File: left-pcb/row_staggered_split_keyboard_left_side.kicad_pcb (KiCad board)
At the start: 2 copper layers, 165 x 132 mm, 177 parts, among them J1 Conn_01x02, SW1 SW_SPST, SW10 SW_SPST, SW11 SW_SPST, SW12 SW_SPST, SW13 SW_SPST, SW14 SW_SPST, SW15 SW_SPST, SW16 SW_SPST, SW17 SW_SPST, SW18 SW_SPST, SW19 SW_SPST, SW2 SW_SPST, SW20 SW_SPST, SW21 SW_SPST, SW22 SW_SPST, SW23 SW_SPST, SW24 SW_SPST, SW25 SW_SPST, SW26 SW_SPST, SW27 SW_SPST, SW28 SW_SPST, SW29 SW_SPST, SW3 SW_SPST, SW30 SW_SPST, SW31 SW_SPST, SW32 SW_SPST, SW33 SW_SPST, SW34 SW_SPST, SW35 SW_SPST, SW36 SW_SPST, SW37 SW_SPST, SW38 SW_SPST, SW39 SW_SPST, SW4 SW_SPST, SW40 SW_SPST, SW41 SW_SPST, SW5 SW_SPST, SW6 SW_SPST, SW7 SW_SPST, SW8 SW_SPST, SW9 SW_SPST, U1 SN74LVC1T45DBV

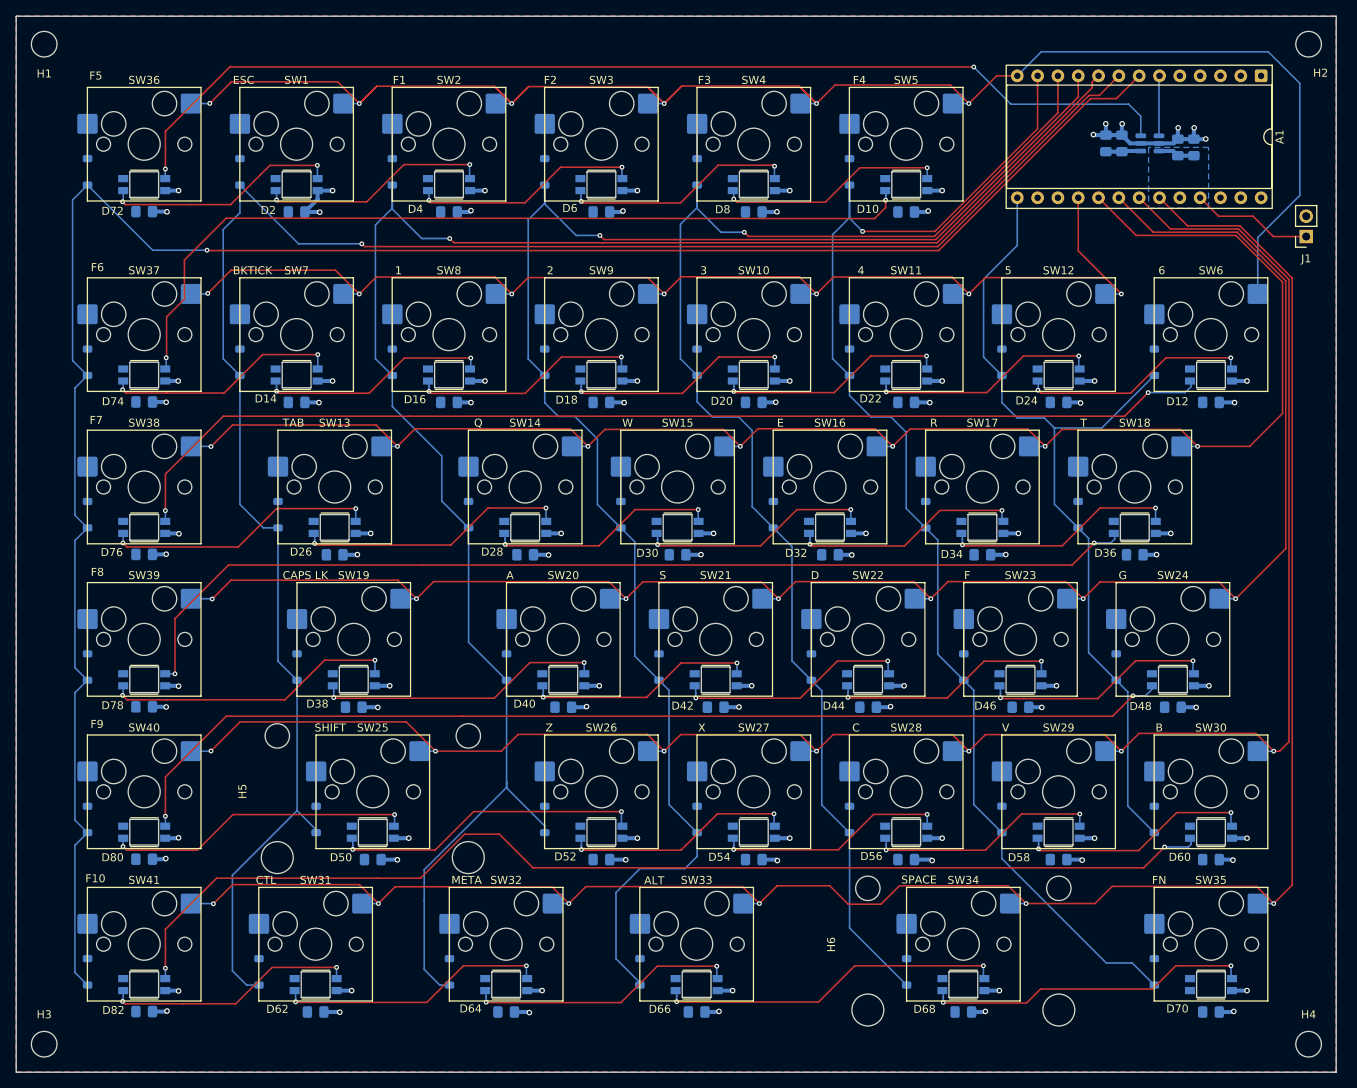
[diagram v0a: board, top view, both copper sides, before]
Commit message: reworking LED data lines to eliminate ground plane disconnections
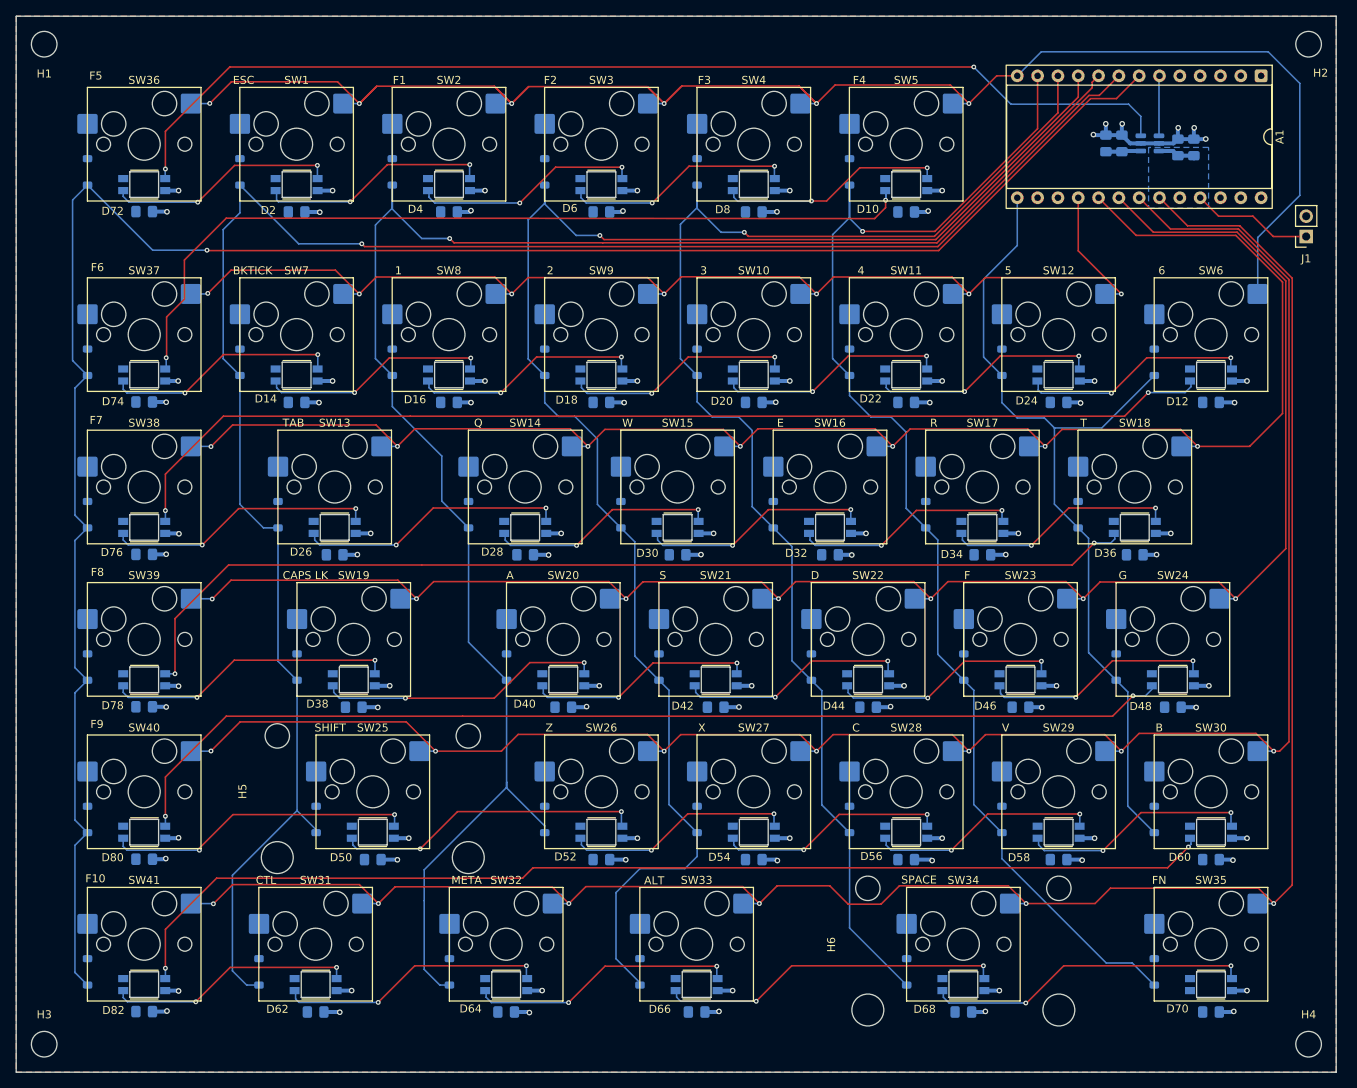
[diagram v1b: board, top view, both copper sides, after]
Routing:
- net /R5C6/DOUT: track 143.0 -> 139.5 mm
- net GND: track 179.3 -> 176.0 mm
- net /R1C0/DOUT: track 29.6 -> 28.9 mm
- net /R6C0/DOUT: track 31.5 -> 31.0 mm
- net /R4C0/DOUT: track 36.8 -> 36.2 mm
- net /R1C3/DOUT: track 29.2 -> 28.7 mm
- net /R4C3/DOUT: track 29.1 -> 28.6 mm

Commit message: duplicate track cleanup and avoiding silkscreen with tracks
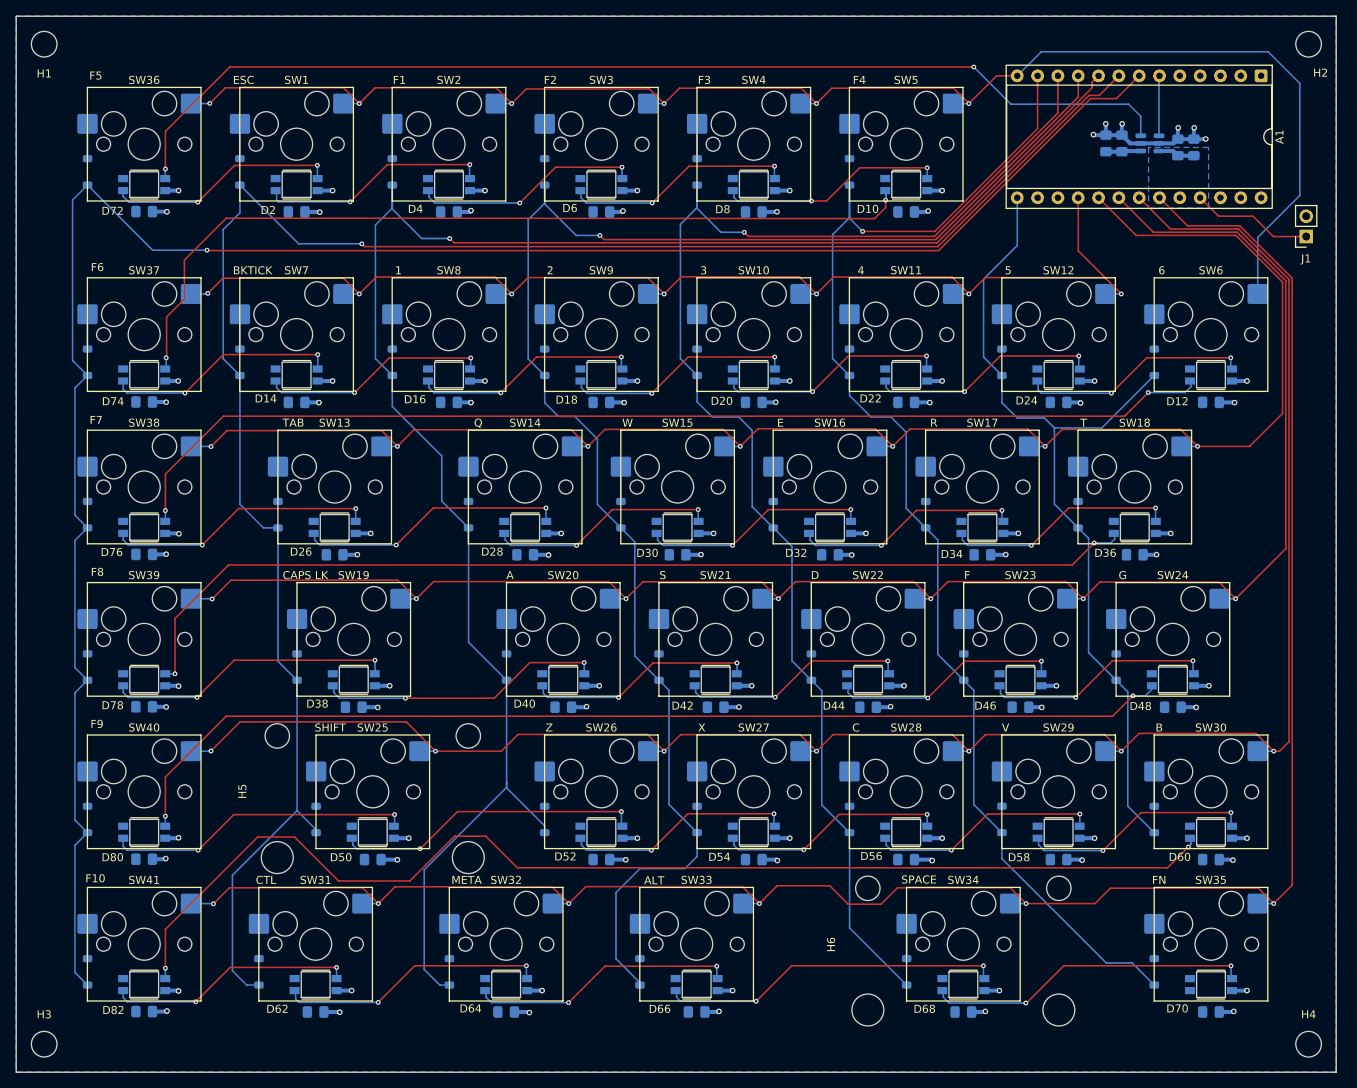
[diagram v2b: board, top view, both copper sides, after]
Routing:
- net /ROW1: track 208.7 -> 189.4 mm
- net /R5C6/DOUT: track 139.5 -> 147.3 mm
- net /ROW2: track 151.0 -> 150.2 mm
- net /ROW3: track 205.1 -> 204.4 mm
- net /ROW6: track 256.0 -> 255.5 mm

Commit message: Silkscreen cleanup and trace cleanup in prep for PCB review posting
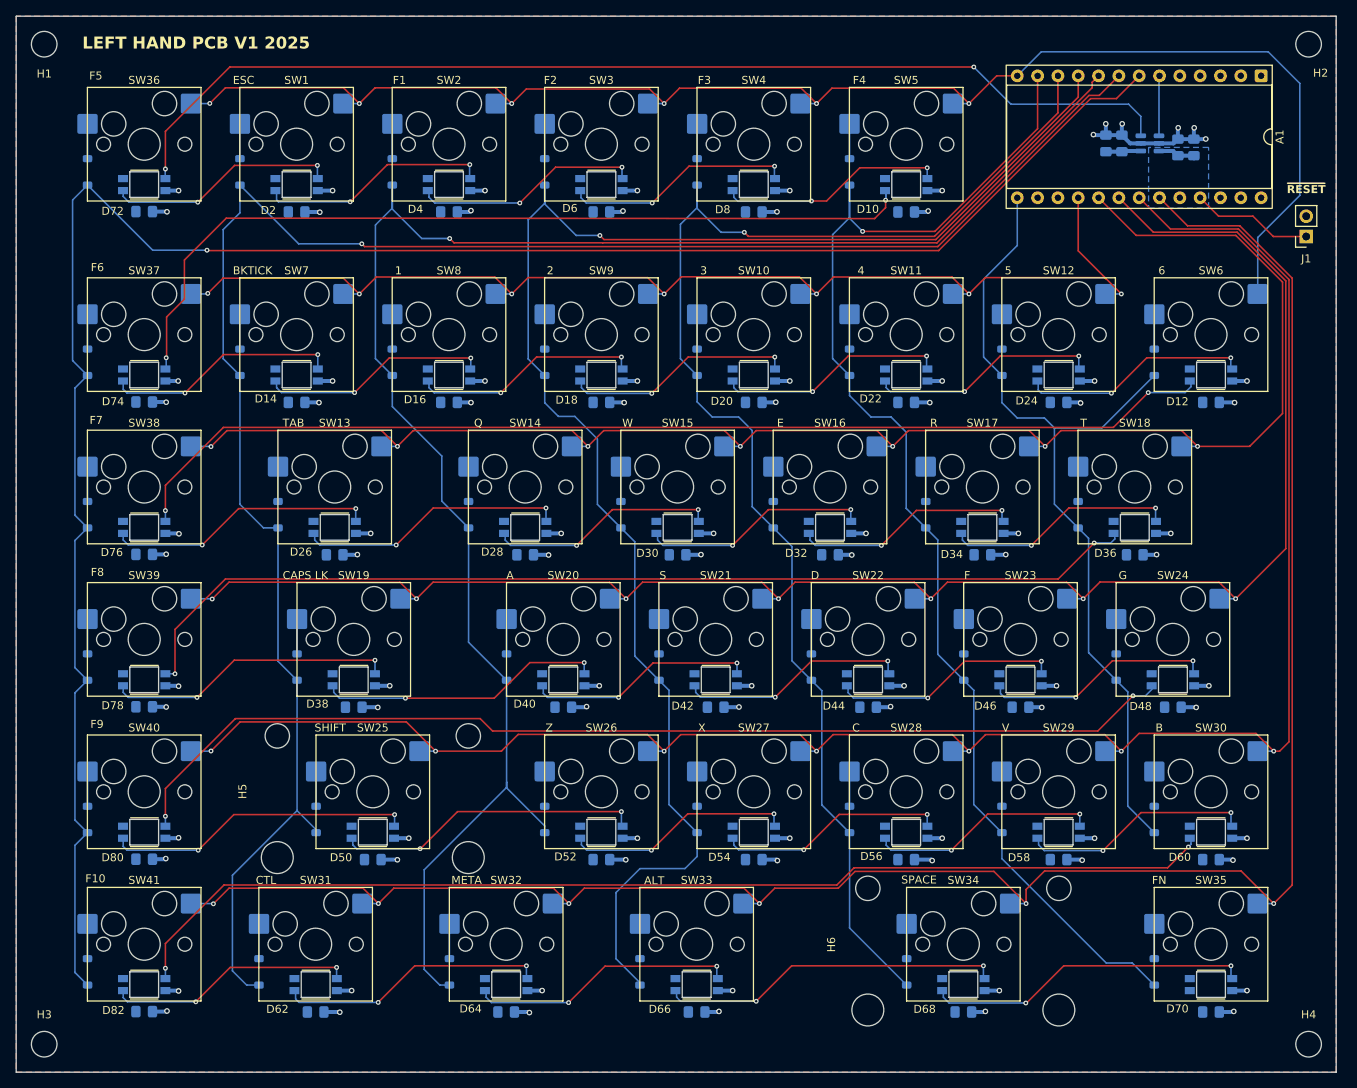
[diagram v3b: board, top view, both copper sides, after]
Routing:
- net /R5C6/DOUT: track 147.3 -> 138.5 mm
- net /ROW6: track 255.5 -> 257.8 mm
- net /R1C6/DOUT: track 139.3 -> 138.5 mm
- net /R3C6/DOUT: track 130.4 -> 129.6 mm
- net /ROW3: track 204.4 -> 203.8 mm
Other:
- board text added: "LEFT HAND PCB V1 2025"
- board text added: "~{RESET}"
